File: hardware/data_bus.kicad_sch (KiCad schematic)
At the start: 11 parts, among them Q13 BC547, U10 74HC595, U11 74HC165, U12 74HC165, U9 74HC595

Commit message: Rev.E. Updated specifications document and hardware design.
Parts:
- Q13: value BC547 -> (none); footprint Package_TO_SOT_THT:TO-92_Inline_Wide -> (none)
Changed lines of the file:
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@@
     (in_bom yes) (on_board yes)
     (property "Reference" "Q13" (id 0) (at 76.2 91.059 90))
-    (property "Value" "BC547" (id 1) (at 76.2 93.3704 90))
-    (property "Footprint" "Package_TO_SOT_THT:TO-92_Inline_Wide" (id 2) (at 74.295 90.17 0)
+    (property "Value" "" (id 1) (at 76.2 93.3704 90))
+    (property "Footprint" "" (id 2) (at 74.295 90.17 0)
       (effects (font (size 1.27 1.27) italic) (justify left) hide)
     )

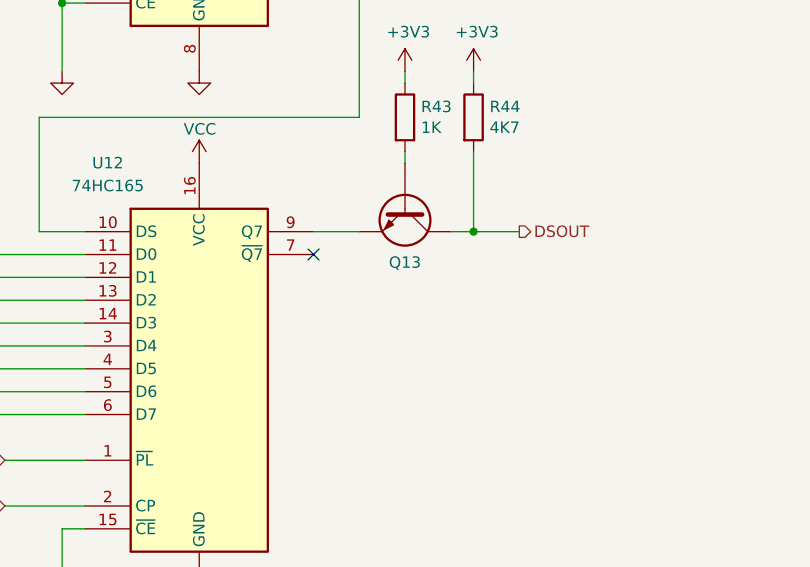
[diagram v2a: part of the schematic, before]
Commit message: Rev.E. Updated R51 wattage.
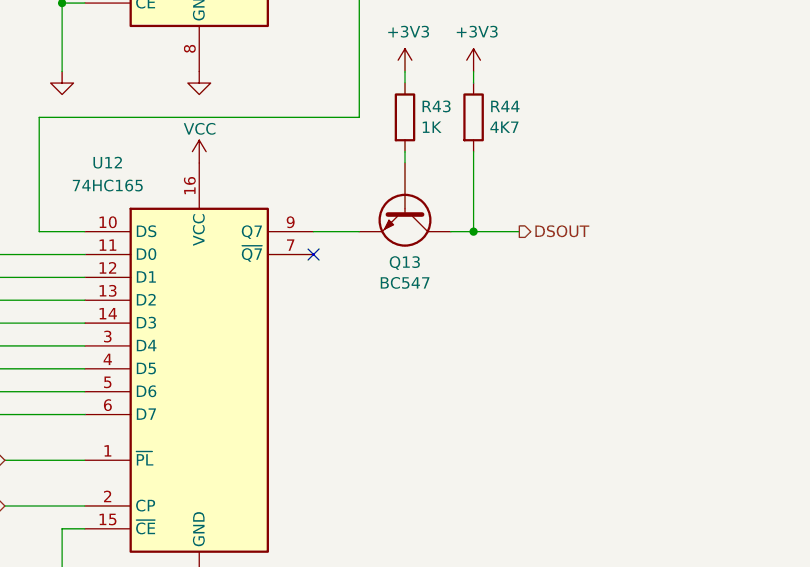
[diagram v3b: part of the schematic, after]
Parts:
- Q13: value (none) -> BC547; footprint (none) -> Package_TO_SOT_THT:TO-92_Inline_Wide
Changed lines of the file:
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@@
     (in_bom yes) (on_board yes)
     (property "Reference" "Q13" (id 0) (at 76.2 91.059 90))
-    (property "Value" "" (id 1) (at 76.2 93.3704 90))
-    (property "Footprint" "" (id 2) (at 74.295 90.17 0)
+    (property "Value" "BC547" (id 1) (at 76.2 93.3704 90))
+    (property "Footprint" "Package_TO_SOT_THT:TO-92_Inline_Wide" (id 2) (at 74.295 90.17 0)
       (effects (font (size 1.27 1.27) italic) (justify left) hide)
     )
